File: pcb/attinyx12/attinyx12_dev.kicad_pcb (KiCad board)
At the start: 2 copper layers, 11 parts, among them J1 Conn_01x06, J2 Conn_01x03, J3 Conn_01x06, J4 Conn_01x06, J5 Conn_01x06, U1 ATtiny212-SS

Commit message: Update attinyx12_dev.kicad_pcb
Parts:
- removed J4, J5: Conn_01x06, Connector_PinHeader_2.54mm:PinHeader_1x06_P2.54mm_Vertical
- removed JP1, JP2: Jumper_2_Bridged, Connector_PinHeader_2.54mm:PinHeader_1x02_P2.54mm_Vertical
- added C2: 100nF, Capacitor_SMD:C_0603_1608Metric, F.Cu at (77.3, 70.0)
- added C3: 100nF, Capacitor_SMD:C_0603_1608Metric, F.Cu at (77.3, 72.5)
- added C4: 1u, Capacitor_SMD:C_0603_1608Metric, F.Cu at (77.3, 75.0)
- added C5: 100nF, Capacitor_SMD:C_0603_1608Metric, F.Cu at (77.3, 77.5)
- added C6: 1u, Capacitor_SMD:C_0603_1608Metric, F.Cu at (77.3, 80.0)
- added D2: LED, LED_SMD:LED_0603_1608Metric, F.Cu at (129.8, 44.5)
- added D3: PMEG6020ER, Diode_SMD:Nexperia_CFP3_SOD-123W, F.Cu at (100.4, 74.1)
- added H1: MountingHole, MountingHole:MountingHole_3.2mm_M3, F.Cu at (31.8, 64.0)
- added H2: MountingHole, MountingHole:MountingHole_3.2mm_M3, F.Cu at (31.8, 72.0)
- added H3: MountingHole, MountingHole:MountingHole_3.2mm_M3, F.Cu at (31.8, 80.0)
- added H4: MountingHole, MountingHole:MountingHole_3.2mm_M3, F.Cu at (31.8, 87.9)
- added R2: 5k1, Resistor_SMD:R_0603_1608Metric, F.Cu at (81.3, 70.0)
- added R3: 27R, Resistor_SMD:R_0603_1608Metric, F.Cu at (81.3, 72.5)
- added R4: 27R, Resistor_SMD:R_0603_1608Metric, F.Cu at (81.3, 75.0)
- added R5: 1k, Resistor_SMD:R_0603_1608Metric, F.Cu at (81.3, 77.5)
- added R6: 0, Resistor_SMD:R_0805_2012Metric, F.Cu at (95.4, 70.7)
- added R7: 0, Resistor_SMD:R_0805_2012Metric, F.Cu at (95.4, 73.7)
- added R8: 470, Resistor_SMD:R_0805_2012Metric, F.Cu at (95.4, 76.6)
- added SW1: SW_Push, Button_Switch_SMD:SW_SPST_CK_RS282G05A3, F.Cu at (132.4, 39.1)
- added SW2: SW_Slide_DPDT, pl_DPDT:MST22D18G_125, F.Cu at (88.9, 74.5)
- added SW3: SW_Push, Button_Switch_SMD:SW_SPST_CK_RS282G05A3, F.Cu at (90.0, 66.7)
- added U2: ATtiny212-SS, Package_SO:SOIC-8_3.9x4.9mm_P1.27mm, F.Cu at (131.0, 31.5)
- added U3: CH342K, Package_SO:SSOP-10-1EP_3.9x4.9mm_P1mm_EP2.1x3.3mm, F.Cu at (114.5, 26.4)
- C1: value 1u -> 1uF; footprint Capacitor_SMD:C_1210_3225Metric_Pad1.33x2.70mm_HandSolder -> Capacitor_SMD:C_0603_1608Metric; moved to F.Cu
- D1: value LED -> PMEG6020ER; footprint LED_THT:LED_D3.0mm -> Diode_SMD:Nexperia_CFP3_SOD-123W
- J1: value Conn_01x06 -> USB_C_Receptacle_USB2.0_16P; footprint Connector_PinHeader_2.54mm:PinHeader_1x06_P2.54mm_Vertical -> Connector_USB:USB_C_Receptacle_G-Switch_GT-USB-7010ASV
- J2: value Conn_01x03 -> Conn_01x06; footprint Connector_PinHeader_2.54mm:PinHeader_1x03_P2.54mm_Vertical -> Connector_PinHeader_2.54mm:PinHeader_1x06_P2.54mm_Vertical; moved to B.Cu
- J3: moved to B.Cu
- R1: value 330 -> 5k1; footprint Resistor_THT:R_Axial_DIN0207_L6.3mm_D2.5mm_P10.16mm_Horizontal -> Resistor_SMD:R_0603_1608Metric
- U1: value ATtiny212-SS -> LM321; footprint Package_SO:SOIC-8_3.9x4.9mm_P1.27mm -> Package_TO_SOT_SMD:SOT-23-5; moved to F.Cu
- moved J3 100.4 mm to (50.8, 36.1), turned to 180 degrees
- moved R1 77.3 mm to (81.3, 67.5)
- moved J2 66.7 mm to (57.2, 35.2)
- moved C1 62.1 mm to (77.3, 67.5), turned to 0 degrees
- moved D1 57.2 mm to (100.4, 70.8)
- moved U1 41.7 mm to (100.2, 78.1), turned to 0 degrees
- moved J1 20.9 mm to (80.0, 30.0), turned to 180 degrees
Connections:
- C1 pad 1: +5V -> VBUS
- D1 pad 1: Net-(D1-K) -> +5V
- D1 pad 2: Net-(D1-A) -> VBUS
- J2 pad 2: /UPDI -> +5V
- J2 pad 3: GND -> +5V
- J3 pad 1: +5V -> GND
- J3 pad 2: +5V -> GND
- J3 pad 3: +5V -> GND
- J3 pad 4: +5V -> /PA3
- J3 pad 5: +5V -> /UPDI
- J3 pad 6: +5V -> /PA2
- R1 pad 1: Net-(D1-K) -> Net-(J1-CC1)
- U1 pad 1: +5V -> /PA3
- U1 pad 2: /TxD -> GND
- U1 pad 3: /RxD -> Net-(D2-A)
- U1 pad 4: /PA1 -> Net-(D2-A)
- U1 pad 5: /PA2 -> +5V
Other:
- board outline added: 30 x 35 mm

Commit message: Update attinyx12_dev.kicad_pcb
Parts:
- removed R6, R7: 0, Resistor_SMD:R_0805_2012Metric
- removed SW1, SW3: SW_Push, Button_Switch_SMD:SW_SPST_CK_RS282G05A3
- removed SW2: SW_Slide_DPDT, pl_DPDT:MST22D18G_125
- added JP1: Jumper_2_Bridged, Jumper:SolderJumper-2_P1.3mm_Bridged_RoundedPad1.0x1.5mm, B.Cu at (47.0, 28.1)
- added JP2: Jumper_2_Bridged, Jumper:SolderJumper-2_P1.3mm_Bridged_RoundedPad1.0x1.5mm, B.Cu at (47.0, 31.6)
- added JP3: Jumper_2_Bridged, Jumper:SolderJumper-2_P1.3mm_Bridged_RoundedPad1.0x1.5mm, B.Cu at (47.0, 35.2)
- H1, H2, H3, H4: footprint MountingHole:MountingHole_3.2mm_M3 -> MountingHole:MountingHole_2.7mm_M2.5
- moved H4 80.8 mm to (88.3, 30.1)
- moved H3 73.1 mm to (102.6, 61.7)
- moved U2 55.0 mm to (80.0, 52.1)
- moved H1 52.4 mm to (71.7, 30.1)
- moved C5 50.6 mm to (110.0, 38.9)
- moved C6 48.0 mm to (109.9, 44.7), turned to 180 degrees
- moved J3 40.0 mm to (85.1, 56.7)
- moved D2 39.9 mm to (112.5, 80.4), turned to 180 degrees
- moved R8 38.8 mm to (110.2, 40.7)
- moved R4 37.1 mm to (79.2, 37.9), turned to -90 degrees
- moved C3 36.9 mm to (99.4, 42.9), turned to 180 degrees
- moved C2 36.3 mm to (112.5, 78.9)
- moved R3 34.6 mm to (80.8, 37.9), turned to -90 degrees
- moved D3 32.9 mm to (110.7, 42.8), turned to 180 degrees
- moved R2 32.3 mm to (77.6, 37.9), turned to -90 degrees
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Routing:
- net VBUS: track 0.00 -> 8.35 mm, vias 0 -> 2
- net Net-(J1-D--PadA7): track 0.00 -> 6.23 mm
- net Net-(J1-D+-PadA6): track 0.00 -> 6.23 mm
- net Net-(J1-CC1): track 0.00 -> 3.83 mm
- net Net-(J1-CC2): track 0.00 -> 3.68 mm
- net GND: track 0.00 -> 2.55 mm, vias 0 -> 2
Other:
- board size 30 x 35 mm -> 30 x 45 mm
- board text added: "5V"
- board text added: "PA1"
- board text added: "PA6"
- board text added: "PA7"

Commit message: Update attinyx12_dev.kicad_pcb
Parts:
- removed the C2 at (112.5, 78.9)
- removed JP1, JP2, JP3: Jumper_2_Bridged, Jumper:SolderJumper-2_P1.3mm_Bridged_RoundedPad1.0x1.5mm
- removed the R3 at (80.8, 37.9)
- removed the R4 at (79.2, 37.9)
- added D1: LED, LED_SMD:LED_0603_1608Metric, F.Cu at (156.5, 20.5)
- added F1: Polyfuse, Fuse:Fuse_0805_2012Metric, F.Cu at (74.8, 37.9)
- added J4: Conn_02x05_Odd_Even, Connector_PinHeader_2.54mm:PinHeader_2x05_P2.54mm_Vertical, F.Cu at (74.9, 57.9)
- added R1: 1k, Resistor_SMD:R_0603_1608Metric, F.Cu at (157.4, 25.3)
- U1: value LM321 -> DT1042-04SO; footprint Package_TO_SOT_SMD:SOT-23-5 -> Package_TO_SOT_SMD:SOT-23-6
- moved U1 66.3 mm to (135.2, 19.1)
- moved C3 40.0 mm to (80.0, 88.5)
- moved J2 40.0 mm to (74.9, 96.7)
- moved J3 40.0 mm to (85.1, 96.7)
- moved U2 40.0 mm to (80.0, 92.1)
- moved D3 36.8 mm to (74.3, 48.5), turned to -90 degrees
- moved R5 34.3 mm to (77.5, 50.8), turned to -90 degrees
- moved D2 34.0 mm to (71.8, 37.9), turned to 90 degrees
- moved H3 33.4 mm to (132.8, 76.0)
- moved H2 22.3 mm to (46.2, 74.8)
- moved C2 19.6 mm to (118.5, 38.2), turned to 90 degrees
- moved C1 18.6 mm to (117.0, 38.2), turned to 90 degrees
- moved C4 15.9 mm to (122.5, 48.9), turned to -90 degrees
- moved U3 13.9 mm to (118.5, 43.5), turned to -90 degrees
- moved C5 7.87 mm to (116.7, 48.8), turned to 90 degrees
- renumbered C3 to C2, C4 to C3, C5 to C4, C6 to C5, D1 to D2, D2 to D4, R1 to R2, R2 to R3, R5 to R4, R8 to R5
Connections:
- C3 pad 1: +5V -> +5VA
- C3 pad 2: GND -> GND1
- D4 pad 2: Net-(D2-A) -> /PA3
- J1 pad A4: VBUS -> Net-(F1-Pad1)
- J1 pad A6: Net-(J1-D+-PadA6) -> /D+
- J1 pad A7: Net-(J1-D--PadA7) -> /D-
- J1 pad A9: VBUS -> Net-(F1-Pad1)
- J1 pad B4: VBUS -> Net-(F1-Pad1)
- J1 pad B6: Net-(J1-D+-PadA6) -> /D+
- J1 pad B7: Net-(J1-D--PadA7) -> /D-
- J1 pad B9: VBUS -> Net-(F1-Pad1)
- J2 pad 1: +5V -> +5VA
- J2 pad 2: +5V -> +5VA
- J2 pad 3: +5V -> +5VA
- J3 pad 1: GND -> GND1
- J3 pad 2: GND -> GND1
- J3 pad 3: GND -> GND1
- R4 pad 2: GND -> GND1
- R5 pad 2: /UPDI -> /UPDI_OUT
- U1 pad 1: /PA3 -> unconnected-(U1-IO1-Pad1)
- U1 pad 3: Net-(D2-A) -> unconnected-(U1-IO2-Pad3)
- U1 pad 4: Net-(D2-A) -> /D+
- U1 pad 5: +5V -> VBUS
- U2 pad 1: +5V -> +5VA
- U2 pad 8: GND -> GND1
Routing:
- net Net-(F1-Pad1): track 0.00 -> 12.2 mm, vias 0 -> 2
- net Net-(J1-D--PadA7): track 6.23 -> 0.00 mm
- net Net-(J1-D+-PadA6): track 6.23 -> 0.00 mm
- net VBUS: track 8.35 -> 4.07 mm, vias 2 -> 0
- net /UPDI_OUT: track 0.00 -> 3.63 mm
- net /D-: track 0.00 -> 2.86 mm
- net /D+: track 0.00 -> 2.86 mm
- added copper zone on B.Cu, net GND
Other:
- board size 30 x 45 mm -> 30 x 85 mm

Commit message: update
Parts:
- moved C4 64.0 mm to (59.4, 37.9), turned to 90 degrees
- moved U3 63.4 mm to (55.5, 36.0)
- moved U1 58.6 mm to (80.0, 38.5), turned to 90 degrees
- moved C5 24.0 mm to (93.2, 43.4), turned to -90 degrees
- moved D2 21.5 mm to (50.3, 36.0)
- moved R5 19.9 mm to (60.1, 41.1)
- moved D3 19.1 mm to (56.9, 40.9), turned to 0 degrees
- moved C2 18.0 mm to (100.9, 42.4), turned to -90 degrees
- moved C1 15.2 mm to (101.8, 37.1), turned to -90 degrees
- moved R2 5.28 mm to (86.6, 34.7)
- moved R3 5.28 mm to (73.4, 34.7)
- moved J4 3.90 mm to (74.9, 54.0)
- moved F1 1.50 mm to (76.2, 38.5)
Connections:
- J4 pad 3: /UPDI -> /PA7
- J4 pad 4: /UPDI_OUT -> /TX
- J4 pad 5: /PA7 -> /PA6
- J4 pad 6: /TX -> /RX
- J4 pad 7: /PA6 -> /UPDI
- J4 pad 8: /RX -> /UPDI_OUT
- U1 pad 4: /D+ -> /D-
- U1 pad 6: /D- -> /D+
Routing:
- net VBUS: track 4.07 -> 0.00 mm
- net Net-(J1-CC1): track 3.83 -> 7.84 mm
- net Net-(F1-Pad1): track 12.2 -> 8.35 mm
- net /UPDI_OUT: track 3.63 -> 0.00 mm
- net Net-(J1-CC2): track 3.68 -> 7.25 mm
- net GND: track 2.55 -> 6.08 mm, vias 2 -> 4
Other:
- board size 30 x 85 mm -> 22.6 x 85 mm

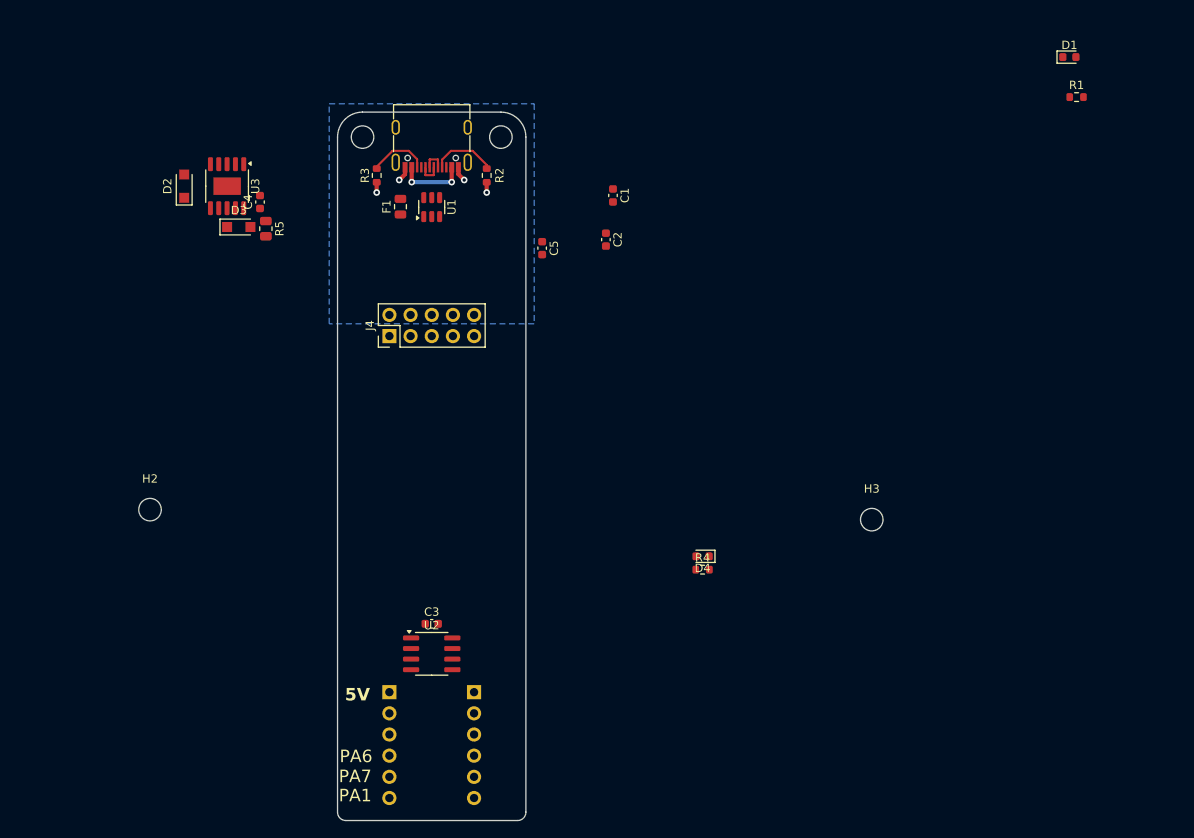
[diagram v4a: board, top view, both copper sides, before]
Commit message: layout programmer side
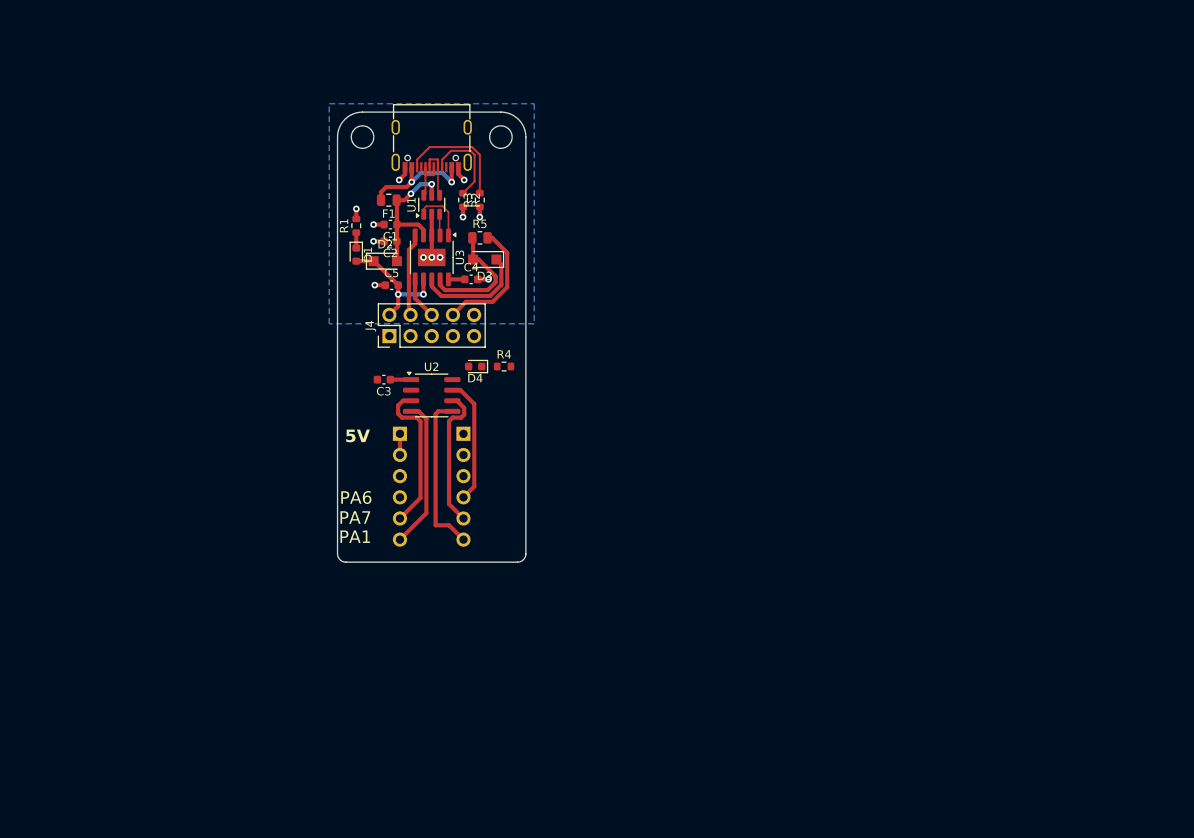
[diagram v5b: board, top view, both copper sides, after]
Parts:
- removed H3, H4: MountingHole, MountingHole:MountingHole_2.7mm_M2.5
- U1: value DT1042-04SO -> USBLC6-2SC6
- moved D1 88.8 mm to (71.0, 44.2), turned to -90 degrees
- moved R1 87.8 mm to (71.0, 40.7), turned to 90 degrees
- moved H2 61.4 mm to (88.3, 30.1)
- moved D4 35.5 mm to (85.2, 57.6)
- moved R4 34.1 mm to (88.7, 57.6)
- moved J2 31.0 mm to (76.2, 65.7)
- moved J3 31.0 mm to (83.8, 65.7)
- moved U2 31.0 mm to (80.0, 61.1)
- moved C3 29.9 mm to (74.3, 59.2), turned to 180 degrees
- moved D3 29.8 mm to (86.4, 44.8), turned to 180 degrees
- moved C4 27.0 mm to (84.7, 47.2), turned to 0 degrees
- moved C1 26.9 mm to (75.0, 40.6), turned to 180 degrees
- moved U3 26.0 mm to (80.0, 44.5)
- moved C2 25.9 mm to (75.0, 42.6), turned to 180 degrees
- moved D2 25.8 mm to (74.4, 45.0), turned to 0 degrees
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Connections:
- U1 pad 1: unconnected-(U1-IO1-Pad1) -> /UD+
- U1 pad 3: unconnected-(U1-IO2-Pad3) -> /UD-
- U3 pad 1: /D+ -> /UD+
- U3 pad 2: /D- -> /UD-
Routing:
- net /PA2: track 0.00 -> 19.5 mm
- net /PA7: track 0.00 -> 18.5 mm
- net /PA1: track 0.00 -> 18.0 mm
- net VBUS: track 0.00 -> 17.8 mm, vias 0 -> 2
- net /UPDI: track 0.00 -> 17.1 mm
- net /UPDI_OUT: track 0.00 -> 15.1 mm
- net /PA3: track 0.00 -> 15.1 mm
- net +5V: track 0.00 -> 15.0 mm, vias 0 -> 2
- net Net-(D3-A): track 0.00 -> 14.9 mm
- net Net-(D3-K): track 0.00 -> 13.5 mm
- net GND: track 6.08 -> 17.5 mm, vias 4 -> 12
- net /TX: track 0.00 -> 9.93 mm
- net /UD+: track 0.00 -> 6.84 mm
- net Net-(J1-CC2): track 7.25 -> 14.0 mm
- net Net-(F1-Pad1): track 8.35 -> 14.4 mm
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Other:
- board size 22.6 x 85 mm -> 22.6 x 54 mm

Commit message: almost there
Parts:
- moved D1 6.76 mm to (71.2, 37.4), turned to 0 degrees
- moved R1 5.27 mm to (71.2, 35.5), turned to 0 degrees
- moved D4 3.33 mm to (87.6, 60.0)
- moved R3 1.58 mm to (84.8, 38.9), turned to 180 degrees
- moved R2 1.29 mm to (84.8, 36.9), turned to 180 degrees
- moved R4 1.16 mm to (87.6, 58.0), turned to 180 degrees
- moved C3 0.50 mm to (74.3, 58.7)
- moved U2 0.50 mm to (80.0, 60.6)
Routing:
- net /PA6: track 0.00 -> 25.3 mm
- net +5VA: track 5.19 -> 24.6 mm
- net /PA7: track 18.5 -> 27.6 mm, vias 0 -> 2
- net /UPDI: track 17.1 -> 25.9 mm
- net +5V: track 15.0 -> 21.0 mm
- net /PA3: track 15.1 -> 20.0 mm, vias 0 -> 1
- net GND1: track 0.00 -> 4.31 mm, vias 0 -> 3
- net Net-(J1-CC2): track 14.0 -> 16.7 mm
- net Net-(D4-K): track 0.00 -> 1.98 mm
- net /PA2: track 19.5 -> 18.7 mm
- added copper zone on B.Cu, net GND1
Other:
- outline, holes or cut-outs redrawn
- board text added: "GND"
- board text added: "PA0"
- board text added: "PA2"
- board text added: "PA3"

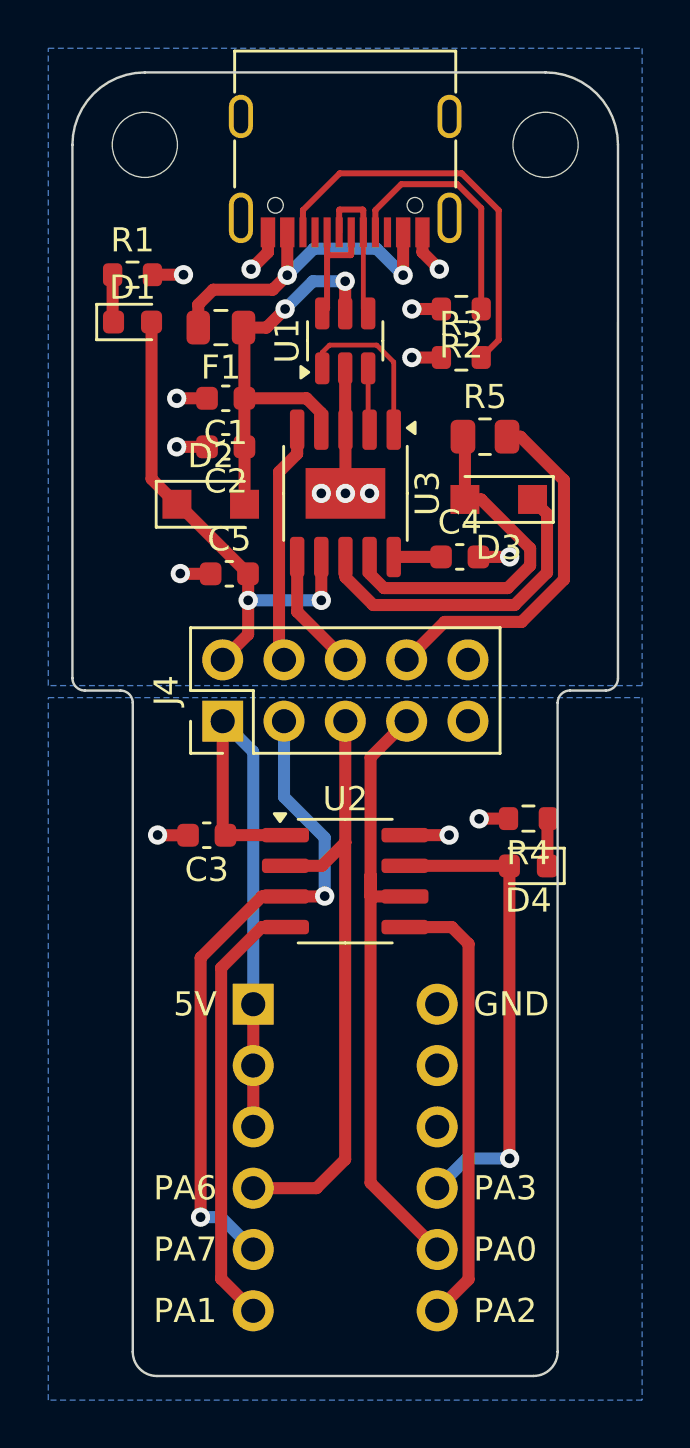
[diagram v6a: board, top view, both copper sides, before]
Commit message: user LED on programmer side
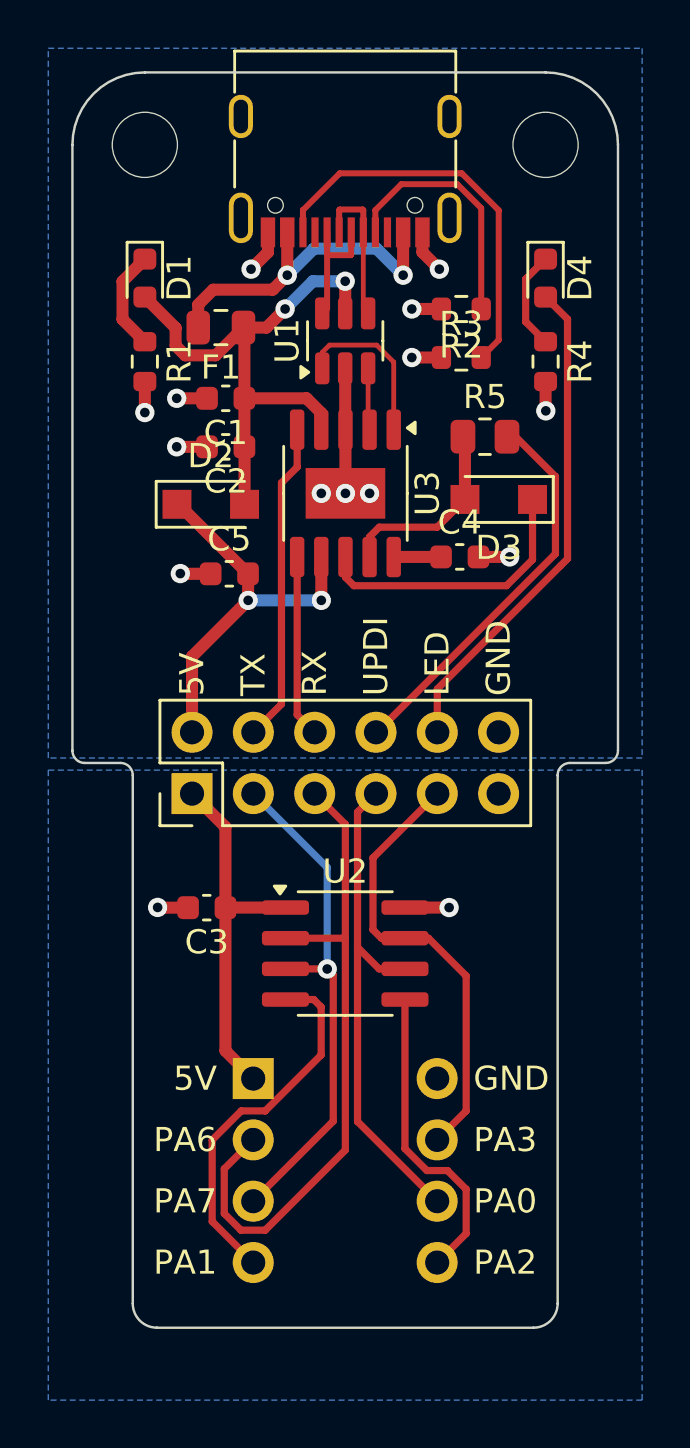
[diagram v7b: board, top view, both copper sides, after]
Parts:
- J2, J3: value Conn_01x06 -> Conn_01x04; footprint Connector_PinHeader_2.54mm:PinHeader_1x06_P2.54mm_Vertical -> Connector_PinHeader_2.54mm:PinHeader_1x04_P2.54mm_Vertical
- J4: value Conn_02x05_Odd_Even -> Conn_02x06; footprint Connector_PinHeader_2.54mm:PinHeader_2x05_P2.54mm_Vertical -> Connector_PinHeader_2.54mm:PinHeader_2x06_P2.54mm_Vertical
- moved D4 24.4 mm to (88.3, 35.6), turned to -90 degrees
- moved R4 18.9 mm to (88.3, 39.1), turned to -90 degrees
- moved R1 3.64 mm to (71.7, 39.1), turned to -90 degrees
- moved J4 3.26 mm to (73.7, 57.0)
- moved J2 3.08 mm to (76.2, 68.8)
- moved J3 3.08 mm to (83.8, 68.8)
- moved C3 3.00 mm to (74.3, 61.7)
- moved U2 3.00 mm to (80.0, 63.6)
- moved D1 1.89 mm to (71.7, 35.6), turned to -90 degrees
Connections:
- D1 pad 2: +5V -> VBUS
- D4 pad 2: /PA3 -> /LED
- J2 pad 2: +5VA -> /PA6
- J2 pad 3: +5VA -> /PA7
- J2 pad 4: /PA6 -> /PA1
- J3 pad 2: GND1 -> /PA3
- J3 pad 3: GND1 -> /PA0
- J3 pad 4: /PA3 -> /PA2
- J4 pad 10: GND -> /LED
- J4 pad 7: /UPDI -> /PA0
- J4 pad 8: /UPDI_OUT -> /UPDI
- J4 pad 9: GND1 -> /PA3
- R4 pad 2: GND1 -> GND
- R5 pad 2: /UPDI_OUT -> /UPDI
- U2 pad 6: /UPDI -> /PA0
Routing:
- net /PA0: track 0.00 -> 20.9 mm
- net /LED: track 0.00 -> 20.6 mm
- net /UPDI_OUT: track 15.1 -> 0.00 mm
- net /UPDI: track 25.9 -> 16.4 mm
- net +5VA: track 24.6 -> 15.5 mm
- net Net-(D3-A): track 14.9 -> 8.06 mm
- net /PA7: track 27.6 -> 21.4 mm, vias 2 -> 1
- net VBUS: track 17.8 -> 23.8 mm
- net /PA2: track 18.7 -> 12.9 mm
- net +5V: track 21.0 -> 16.5 mm
- net /TX: track 9.93 -> 13.3 mm
- net /PA1: track 18.1 -> 15.4 mm
- net /PA6: track 25.3 -> 28.0 mm
- net /RX: track 5.09 -> 7.56 mm
- net Net-(D1-K): track 1.98 -> 4.19 mm
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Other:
- board size 22.6 x 54 mm -> 22.6 x 52 mm
- board text added: "LED"
- board text added: "RX"
- board text added: "TX"
- board text added: "UPDI"
